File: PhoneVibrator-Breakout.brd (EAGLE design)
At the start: 8.6 x 8.9 mm, 2 parts

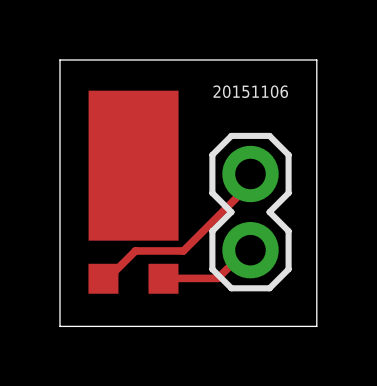
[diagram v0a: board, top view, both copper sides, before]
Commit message: Fixed issue with where I placed the mechanical pad
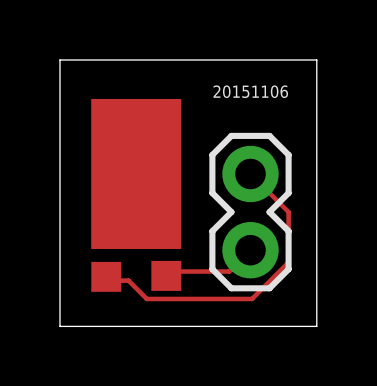
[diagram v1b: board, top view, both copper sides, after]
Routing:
- net N$1: track 6.60 -> 10.4 mm
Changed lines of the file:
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@@
 <wire x1="0" y1="8.88" x2="0" y2="0" width="0" layer="20"/>
 <text x="5.08" y="7.62" size="0.4064" layer="21">20151106</text>
-<text x="3.81" y="7.62" size="1.6764" layer="22" rot="MR270">Buzzz</text>
+<text x="2.54" y="7.62" size="1.27" layer="22" rot="MR270">Buzzz</text>
 </plain>
 <attributes>
@@
 </class>
 </classes>
-<designrules name="default">
+<designrules name="LaenPCBOrder">
 <description language="de">&lt;b&gt;EAGLE Design Rules&lt;/b&gt;
 &lt;p&gt;
@@
 Einstellungen hier und speichern die Design Rules unter
 einem neuen Namen ab.</description>
-<description language="en">&lt;b&gt;EAGLE Design Rules&lt;/b&gt;
+<description language="en">&lt;b&gt;Laen's PCB Order Design Rules&lt;/b&gt;
 &lt;p&gt;
-The default Design Rules have been set to cover
-a wide range of applications. Your particular design
-may have different requirements, so please make the
-necessary adjustments and save your customized
-design rules under a new name.</description>
+Please make sure your boards conform to these design rules.</description>
 <param name="layerSetup" value="(1*16)"/>
-<param name="mtCopper" value="0.035mm 0.035mm 0.035mm 0.035mm 0.035mm 0.035mm 0.035mm 0.035mm 0.035mm 0.035mm 0.035mm 0.035mm 0.035mm 0.035mm 0.035mm 0.035mm"/>
-<param name="mtIsolate" value="1.5mm 0.15mm 0.2mm 0.15mm 0.2mm 0.15mm 0.2mm 0.15mm 0.2mm 0.15mm 0.2mm 0.15mm 0.2mm 0.15mm 0.2mm"/>
-<param name="mdWireWire" value="8mil"/>
-<param name="mdWirePad" value="8mil"/>
-<param name="mdWireVia" value="8mil"/>
-<param name="mdPadPad" value="8mil"/>
-<param name="mdPadVia" value="8mil"/>
-<param name="mdViaVia" value="8mil"/>
-<param name="mdSmdPad" value="8mil"/>
-<param name="mdSmdVia" value="8mil"/>
-<param name="mdSmdSmd" value="8mil"/>
+<param name="mtCopper" value="0.0356mm 0.0356mm 0.0356mm 0.0356mm 0.0356mm 0.0356mm 0.0356mm 0.0356mm 0.0356mm 0.0356mm 0.0356mm 0.0356mm 0.0356mm 0.0356mm 0.0356mm 0.0356mm"/>
+<param name="mtIsolate" value="1.5011mm 0.1499mm 0.2007mm 0.1499mm 0.2007mm 0.1499mm 0.2007mm 0.1499mm 0.2007mm 0.1499mm 0.2007mm 0.1499mm 0.2007mm 0.1499mm 0.2007mm"/>
+<param name="mdWireWire" value="6mil"/>
+<param name="mdWirePad" value="6mil"/>
+<param name="mdWireVia" value="6mil"/>
+<param name="mdPadPad" value="6mil"/>
+<param name="mdPadVia" value="6mil"/>
+<param name="mdViaVia" value="6mil"/>
+<param name="mdSmdPad" value="6mil"/>
+<param name="mdSmdVia" value="6mil"/>
+<param name="mdSmdSmd" value="6mil"/>
 <param name="mdViaViaSameLayer" value="8mil"/>
 <param name="mnLayersViaInSmd" value="2"/>
-<param name="mdCopperDimension" value="40mil"/>
-<param name="mdDrill" value="8mil"/>
+<param name="mdCopperDimension" value="15mil"/>
+<param name="mdDrill" value="6mil"/>
 <param name="mdSmdStop" value="0mil"/>
-<param name="msWidth" value="10mil"/>
-<param name="msDrill" value="24mil"/>
-<param name="msMicroVia" value="9.99mm"/>
+<param name="msWidth" value="6mil"/>
+<param name="msDrill" value="13mil"/>
+<param name="msMicroVia" value="13mil"/>
 <param name="msBlindViaRatio" value="0.5"/>
 <param name="rvPadTop" value="0.25"/>
@@
 <param name="rvMicroViaOuter" value="0.25"/>
 <param name="rvMicroViaInner" value="0.25"/>
-<param name="rlMinPadTop" value="10mil"/>
+<param name="rlMinPadTop" value="7mil"/>
 <param name="rlMaxPadTop" value="20mil"/>
-<param name="rlMinPadInner" value="10mil"/>
+<param name="rlMinPadInner" value="7mil"/>
 <param name="rlMaxPadInner" value="20mil"/>
-<param name="rlMinPadBottom" value="10mil"/>
+<param name="rlMinPadBottom" value="7mil"/>
 <param name="rlMaxPadBottom" value="20mil"/>
-<param name="rlMinViaOuter" value="8mil"/>
+<param name="rlMinViaOuter" value="7mil"/>
 <param name="rlMaxViaOuter" value="20mil"/>
-<param name="rlMinViaInner" value="8mil"/>
+<param name="rlMinViaInner" value="7mil"/>
 <param name="rlMaxViaInner" value="20mil"/>
 <param name="rlMinMicroViaOuter" value="4mil"/>
@@
 <param name="mvStopFrame" value="1"/>
 <param name="mvCreamFrame" value="0"/>
-<param name="mlMinStopFrame" value="4mil"/>
-<param name="mlMaxStopFrame" value="4mil"/>
+<param name="mlMinStopFrame" value="3mil"/>
+<param name="mlMaxStopFrame" value="3mil"/>
 <param name="mlMinCreamFrame" value="0mil"/>
 <param name="mlMaxCreamFrame" value="0mil"/>
@@
 <param name="RoutingGrid" value="50mil"/>
 <param name="AutoGrid" value="1"/>
-<param name="Efforts" value="0"/>
+<param name="Efforts" value="2"/>
 <param name="TopRouterVariant" value="1"/>
 <param name="tpViaShape" value="round"/>
@@
 <contactref element="U$1" pad="P$1"/>
 <contactref element="JP1" pad="1"/>
-<wire x1="2.5146" y1="2.5146" x2="1.6002" y2="1.6002" width="0.254" layer="1"/>
-<wire x1="4.1148" y1="2.5146" x2="2.5146" y2="2.5146" width="0.254" layer="1"/>
-<wire x1="6.1722" y1="4.572" x2="4.1148" y2="2.5146" width="0.254" layer="1"/>
-<wire x1="6.1722" y1="5.0292" x2="6.1722" y2="4.572" width="0.254" layer="1"/>
-<wire x1="1.6002" y1="1.6002" x2="1.4481375" y2="1.5875" width="0.254" layer="1"/>
-<wire x1="6.1722" y1="5.0292" x2="6.35" y2="5.08" width="0.254" layer="1"/>
+<wire x1="2.286" y1="1.524" x2="1.6764" y2="1.524" width="0.1524" layer="1"/>
+<wire x1="2.8956" y1="0.9144" x2="2.286" y2="1.524" width="0.1524" layer="1"/>
+<wire x1="6.4008" y1="0.9144" x2="2.8956" y2="0.9144" width="0.1524" layer="1"/>
+<wire x1="7.62" y1="2.1336" x2="6.4008" y2="0.9144" width="0.1524" layer="1"/>
+<wire x1="7.62" y1="3.81" x2="7.62" y2="2.1336" width="0.1524" layer="1"/>
+<wire x1="6.35" y1="5.08" x2="7.62" y2="3.81" width="0.1524" layer="1"/>
+<wire x1="1.6764" y1="1.524" x2="1.5433875" y2="1.651" width="0.1524" layer="1"/>
 </signal>
 <signal name="N$2">
 <contactref element="U$1" pad="P$2"/>
 <contactref element="JP1" pad="2"/>
-<wire x1="5.2578" y1="1.6002" x2="3.6576" y2="1.6002" width="0.254" layer="1"/>
-<wire x1="6.1722" y1="2.5146" x2="5.2578" y2="1.6002" width="0.254" layer="1"/>
-<wire x1="3.6576" y1="1.6002" x2="3.44961875" y2="1.5875" width="0.254" layer="1"/>
-<wire x1="6.1722" y1="2.5146" x2="6.35" y2="2.54" width="0.254" layer="1"/>
+<wire x1="5.6388" y1="1.8288" x2="3.6576" y2="1.8288" width="0.1524" layer="1"/>
+<wire x1="6.35" y1="2.54" x2="5.6388" y2="1.8288" width="0.1524" layer="1"/>
+<wire x1="3.6576" y1="1.8288" x2="3.54486875" y2="1.68275" width="0.1524" layer="1"/>
 </signal>
 </signals>
